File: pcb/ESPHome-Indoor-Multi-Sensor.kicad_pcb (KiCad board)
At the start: 4 copper layers, 52.5 x 59.7 mm, 108 parts, among them J1 SEN66, J2 USB-C, J3 SEN0609, J4 LD2410, J5 SPKR, J6 LD2450, Q1 MMBFJ201, SW1 BOOT, SW2 RESET, U1 TPS22917DBV, U10 TSL2591, U11 SGP41, U12 SCD41, U13 BMP581, U14 MCP6042, U15 ADS1115, U16 SHT45, U17 EKMC1603111, U18 TGS5141, U2 TPS22917DBV, U3 SN74LV1T34DBV, U4 TLV62568DRL, U5 MAX98357A, U6 TLV75533PDRV, U7 TLV62568DRL, U8 ESP32-S3-WROOM-2-N32R16V, U9 INA228

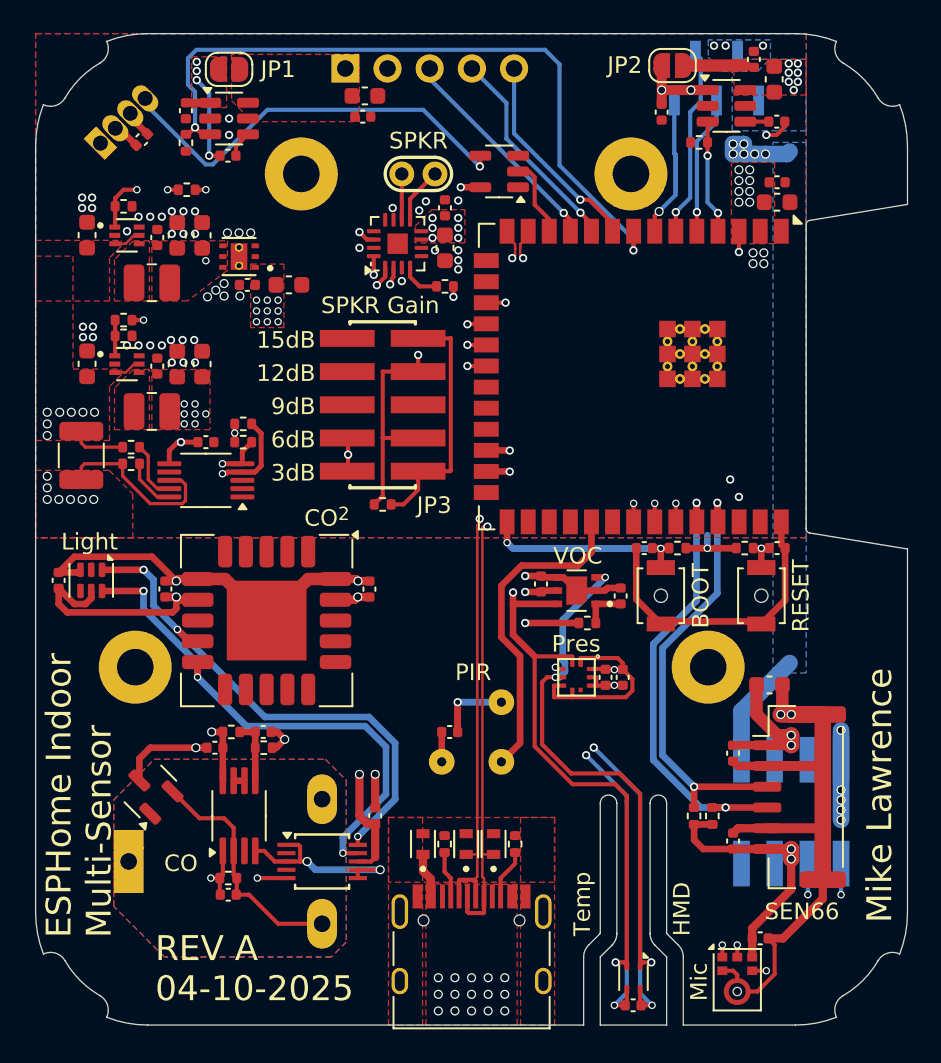
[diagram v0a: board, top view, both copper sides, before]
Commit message: Rev A Updates
Support LD2410S and LD2420 Radars in same connector as C4001. Now using 3.3V instead of 5V.
Removed Power control for Radars.
Added DS18S20 to measure CO sensor temperature directly.
Reworked SHT4X layout to reduce thermal transfer.
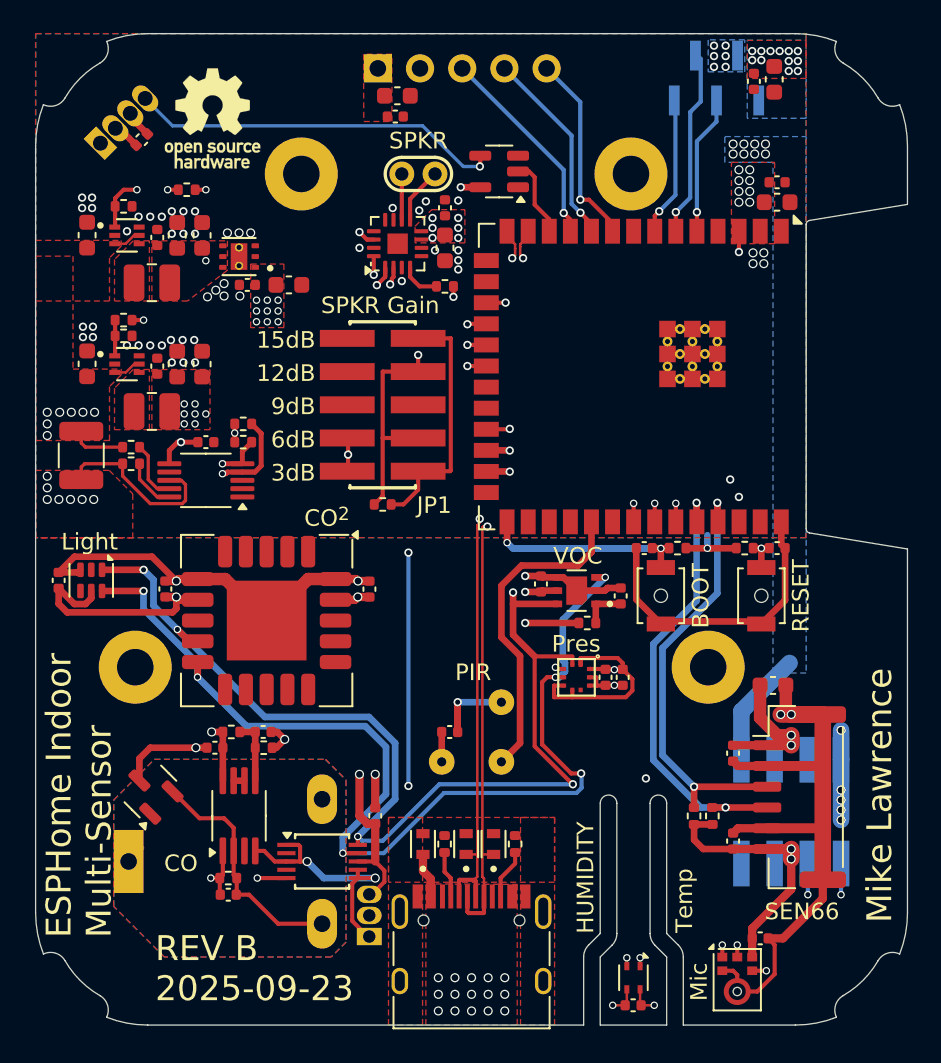
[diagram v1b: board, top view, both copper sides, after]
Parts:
- removed the C4 at (104.5, 37.4)
- removed the C5 at (133.2, 37.5)
- removed the C7 at (140.1, 38.1)
- removed the C9 at (107.1, 40.1)
- removed the JP1 at (107.2, 35.0)
- removed JP2: ~, Jumper:SolderJumper-2_P1.3mm_Open_RoundedPad1.0x1.5mm
- removed the R1 at (104.5, 39.4)
- removed the R2 at (135.5, 39.4)
- removed the U2 at (107.2, 37.9)
- added T1: Tab, KiKit:Tab, F.Cu at (114.7, 32.5)
- added T10: Tab, KiKit:Tab, F.Cu at (138.5, 92.8)
- added T2: Tab, KiKit:Tab, F.Cu at (131.5, 32.5)
- added T3: Tab, KiKit:Tab, F.Cu at (138.5, 32.5)
- added T4: Tab, KiKit:Tab, F.Cu at (95.2, 41.2)
- added T5: Tab, KiKit:Tab, F.Cu at (148.3, 41.2)
- added T6: Tab, KiKit:Tab, F.Cu at (95.2, 75.8)
- added T7: Tab, KiKit:Tab, F.Cu at (148.3, 75.8)
- added T8: Tab, KiKit:Tab, F.Cu at (114.7, 92.8)
- added T9: Tab, KiKit:Tab, F.Cu at (131.5, 92.8)
- added TEXT0: OSHW-Logo_5.7x6mm_SilkScreen, Symbol:OSHW-Logo_5.7x6mm_SilkScreen, F.Cu at (106.2, 37.9)
- U17: renamed from U1; value TPS22917DBV -> DS18S20; footprint Package_TO_SOT_SMD:SOT-23-6 -> Package_TO_SOT_THT:TO-92_Inline; moved to B.Cu
- moved U17 54.4 mm to (115.6, 87.2), turned to 90 degrees
- moved C3 1.96 mm to (117.3, 36.5)
- moved C4 1.96 mm to (117.2, 37.8)
- moved J3 1.96 mm to (116.1, 34.9)
- moved C1 1.32 mm to (138.8, 35.7), turned to -90 degrees
- moved C30 0.21 mm to (139.9, 72.0)
- renumbered C14 to C10, C15 to C11, C16 to C12, C17 to C13, C18 to C14, C19 to C15, C20 to C16, C21 to C17, C22 to C18, C23 to C19, C24 to C20, C25 to C21, C26 to C22, C27 to C23, C28 to C24, C29 to C25, C30 to C26, C31 to C27, C32 to C28, C33 to C29, C34 to C30, C35 to C31, C36 to C32, C37 to C33, C38 to C34, C39 to C35, C40 to C36, C41 to C37, C42 to C38, C43 to C39, C6 to C4, C8 to C5, C10 to C6, C11 to C7, C12 to C8, C13 to C9, JP3 to JP1, MH4 to MH3, MH3 to MH4, R3 to R1, R12 to R10, R13 to R11, R14 to R12, R15 to R13, R16 to R14, R17 to R15, R18 to R16, R23 to R17, R22 to R18, R4 to R2, R5 to R3, R6 to R4, R7 to R5, R8 to R6, R9 to R7, R10 to R8, R11 to R9, TEXT1 to TEXT0, U3 to U1, U12 to U10, U13 to U11, U14 to U12, U15 to U13, U16 to U14, U17 to U15, U18 to U16, U4 to U2, U5 to U3, U6 to U4, U7 to U5, U8 to U6, U9 to U7, U10 to U8, U11 to U9
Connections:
- net /LD24X0_OUT renamed /RDRB_OUT
- net /LD24X0_RX renamed /RDRB_RX
- net /LD24X0_TX renamed /RDRB_TX
- net /SEN0609_OUT renamed /RDRA_OUT
- net /SEN0609_RX renamed /RDRA_SIG2
- net /SEN0609_TX renamed /RDRA_SIG1
- C1 pad 1: /Presence Sensors/LD24X0_VCC -> +5V
- C2 pad 1: /Presence Sensors/LD24X0_VCC -> +5V
- C3 pad 1: /Presence Sensors/SENS0609_VCC -> +3.3V
- C4 pad 1: /Presence Sensors/SENS0609_VCC -> +3.3V
- J3 pad 1: /Presence Sensors/SENS0609_VCC -> +3.3V
- J4 pad 5: /Presence Sensors/LD24X0_VCC -> +5V
- J6 pad 8: /Presence Sensors/LD24X0_VCC -> +5V
- U17 pad 1: +5V -> GND
- U17 pad 2: GND -> /1Wire
- U17 pad 3: /LD24X0_EN -> +3.3VA
- U6 pad 23: unconnected-(U8-IO21-Pad23) -> /1Wire
- U6 pad 4: /LD24X0_EN -> /ESP32-S3/LD24X0_EN
- U6 pad 8: /SEN0609_EN -> /ESP32-S3/SEN0609_EN
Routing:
- net /SEN0609_EN: track 43.3 -> 0.00 mm, vias 2 -> 0
- net /1Wire: track 0.00 -> 36.8 mm, vias 0 -> 3
- net /Presence Sensors/LD24X0_VCC: track 19.3 -> 0.00 mm, vias 12 -> 0
- net /SDA1: track 121.0 -> 105.7 mm, vias 8 -> 9
- net /SCL1: track 115.1 -> 101.5 mm, vias 7 -> 8
- net /LD24X0_EN: track 6.87 -> 0.00 mm, vias 2 -> 0
- net +5V: track 49.7 -> 46.3 mm, vias 22 -> 32
- net Net-(D4-DIN): track 25.4 -> 22.5 mm
- net +3.3VA: track 113.0 -> 115.7 mm, vias 23 -> 22
- net /RDRB_OUT: track 10.8 -> 8.42 mm
- net Net-(U2-CT): track 1.59 -> 0.00 mm
- net Net-(U1-CT): track 1.41 -> 0.00 mm
- net /RDRA_OUT: track 12.6 -> 11.8 mm
- net /RDRA_SIG1: track 13.2 -> 12.4 mm
- net /RDRA_SIG2: track 13.3 -> 12.5 mm
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- added copper zone on B.Cu, net +5V
- removed copper zone on B.Cu, net /Presence Sensors/LD24X0_VCC
- removed copper zone on F.Cu, net /Presence Sensors/LD24X0_VCC
- removed copper zone on In2.Cu, net /Presence Sensors/LD24X0_VCC
- removed copper zone on F.Cu, net /Presence Sensors/SENS0609_VCC
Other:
- outline, holes or cut-outs redrawn
- board text added: "HUMIDITY"
- board text added: "LD2410b"
- board text added: "REV B 2025-09-23"
- board text added: "SEN0609 LD2410S LD2420"
- board text removed: "HMD"
- board text removed: "LD2410"
- board text removed: "REV A 04-10-2025"
- board text removed: "SEN0609"
